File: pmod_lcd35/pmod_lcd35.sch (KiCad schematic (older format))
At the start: 20 parts

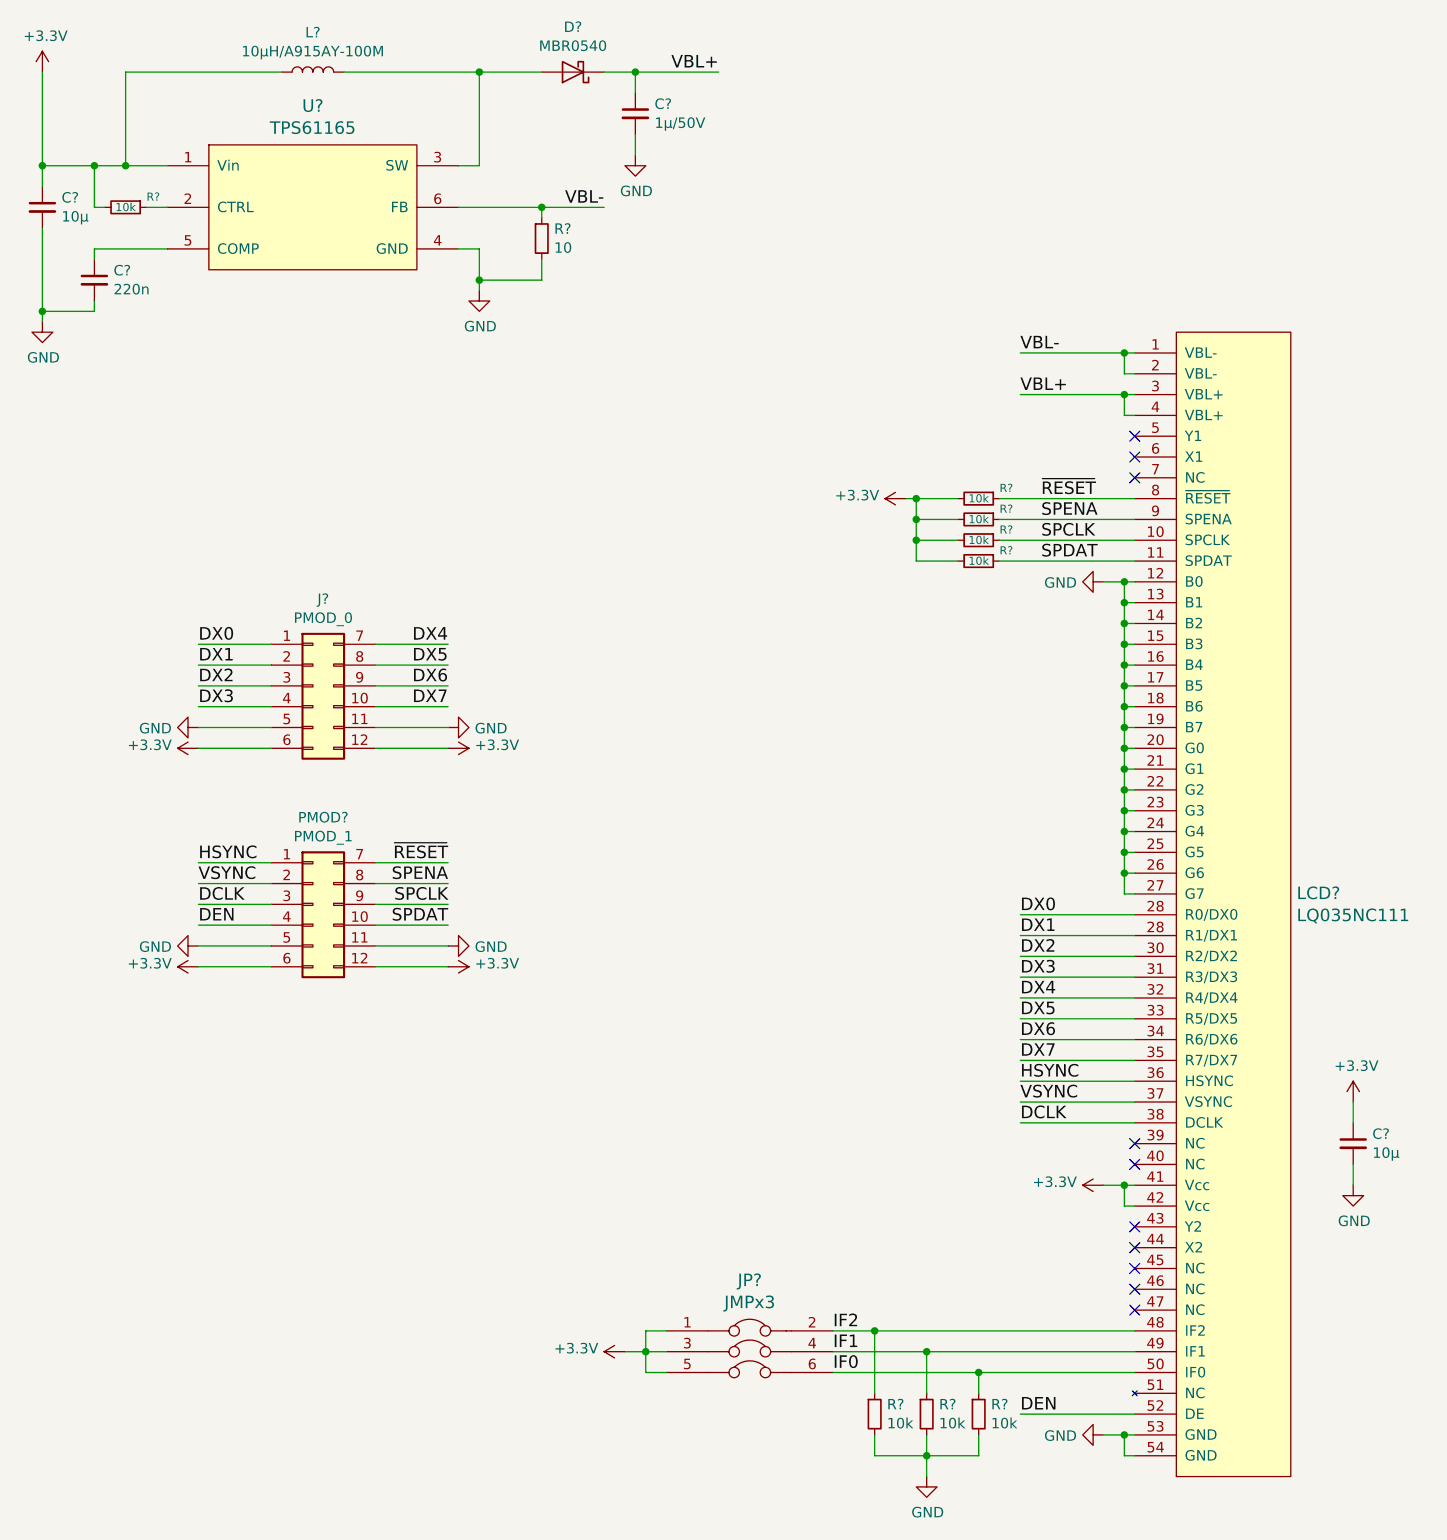
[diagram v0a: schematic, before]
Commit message: LCD PMOD PCB ready to route
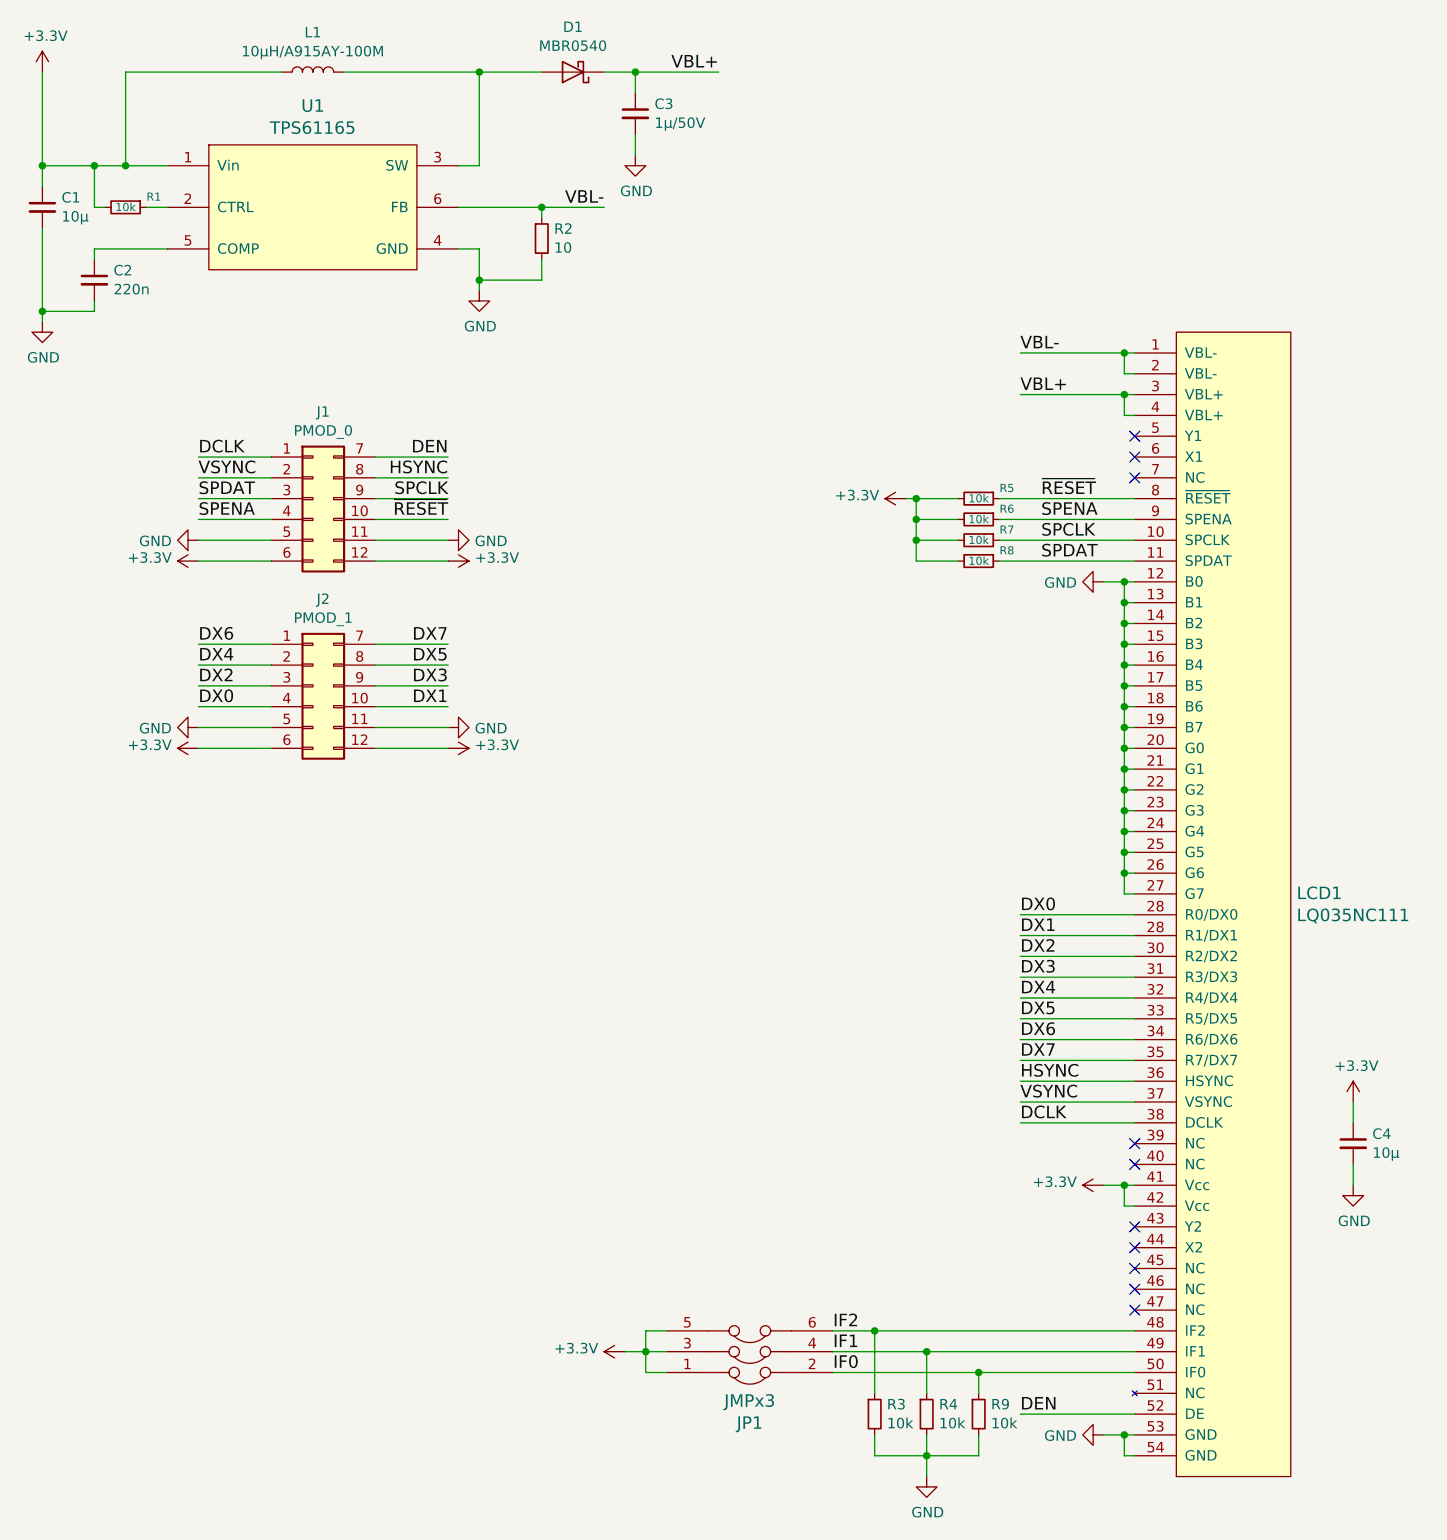
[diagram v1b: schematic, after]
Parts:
- C1, C3, C4: renamed from C?; footprint (none) -> Capacitors_SMD:C_0805
- C2: renamed from C?; footprint (none) -> Capacitors_SMD:C_0603
- D1: renamed from D?; footprint (none) -> Diodes_SMD:D_SOD-123
- J1: renamed from J?; footprint (none) -> Custom Parts:PMOD_2x06_2.54mm
- J2: renamed from PMOD?; footprint (none) -> Custom Parts:PMOD_2x06_2.54mm
- JP1: renamed from JP?; footprint (none) -> Pin_Headers:Pin_Header_Straight_2x03_Pitch2.54mm
- L1: renamed from L?; footprint (none) -> Custom Parts:muRata_L_2020
- LCD1: renamed from LCD?; footprint (none) -> Custom Parts:MOLEX_51296-5494_54pin_0.5mm_BTM
- R1, R2, R3, R4, R5, R6, R7, R8, R9: renamed from R?; footprint (none) -> Resistors_SMD:R_0603
- U1: renamed from U?; footprint (none) -> TO_SOT_Packages_SMD:SOT-23-6
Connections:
- net DCLK: now also J1.1 (Pin_1); no longer J2.3 (Pin_3)
- net DEN: now also J1.7 (Pin_7); no longer J2.4 (Pin_4)
- net DX0: now also J2.4 (Pin_4); no longer J1.1 (Pin_1)
- net DX1: now also J2.10 (Pin_10); no longer J1.2 (Pin_2)
- net DX2: now also J2.3 (Pin_3); no longer J1.3 (Pin_3)
- net DX3: now also J2.9 (Pin_9); no longer J1.4 (Pin_4)
- net DX4: now also J2.2 (Pin_2); no longer J1.7 (Pin_7)
- net DX5: now also J2.8 (Pin_8); no longer J1.8 (Pin_8)
- net DX6: now also J2.1 (Pin_1); no longer J1.9 (Pin_9)
- net DX7: now also J2.7 (Pin_7); no longer J1.10 (Pin_10)
- net HSYNC: now also J1.8 (Pin_8); no longer J2.1 (Pin_1)
- net IF0: now also JP1.2; no longer JP1.6
- net IF2: now also JP1.6; no longer JP1.2
- net SPCLK: now also J1.9 (Pin_9); no longer J2.9 (Pin_9)
- net SPDAT: now also J1.3 (Pin_3); no longer J2.10 (Pin_10)
- net SPENA: now also J1.4 (Pin_4); no longer J2.8 (Pin_8)
- net VSYNC: now also J1.2 (Pin_2); no longer J2.2 (Pin_2)
- net ~RESET: now also J1.10 (Pin_10); no longer J2.7 (Pin_7)
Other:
- moved on the sheet: J1, J2
